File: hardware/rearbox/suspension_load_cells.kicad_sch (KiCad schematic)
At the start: 16 parts, among them U31 NAU7802SGI

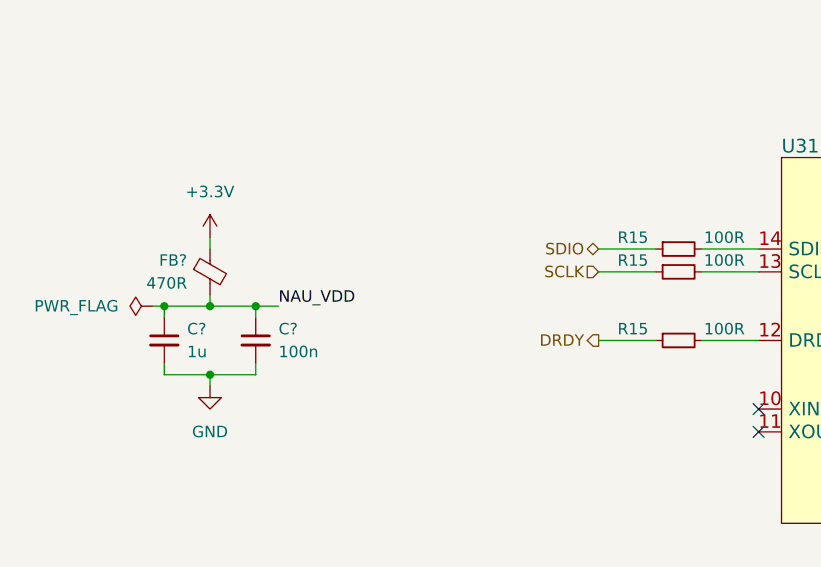
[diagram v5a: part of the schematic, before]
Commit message: Route the tracks on the connector PCB
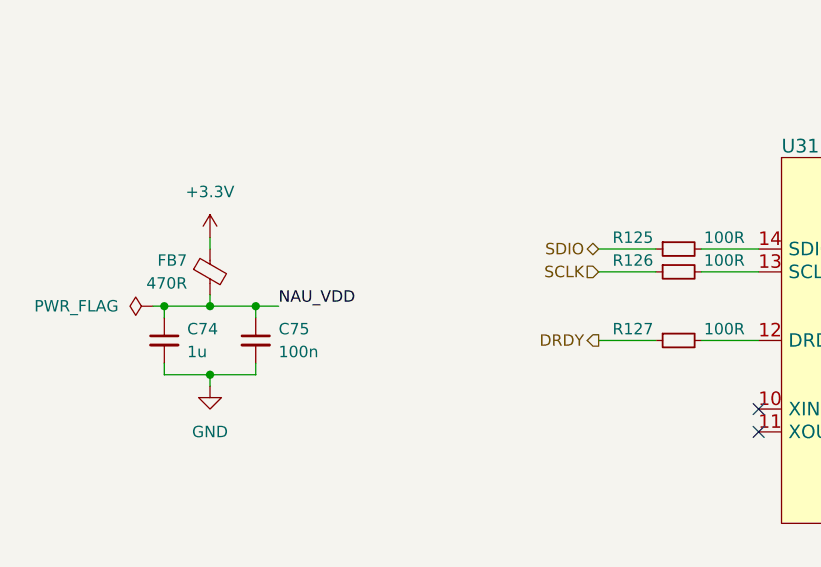
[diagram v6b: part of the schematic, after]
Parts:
- gave numbers to parts that had none: 3
- renumbered R15 to R125, R15 to R126, R15 to R127
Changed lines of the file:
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@@
   (symbol (lib_id "Device:C_Small") (at 74.93 102.87 0) (unit 1)
     (in_bom yes) (on_board yes) (dnp no)
-    (property "Reference" "C?" (at 77.47 101.6 0)
+    (property "Reference" "C75" (at 77.47 101.6 0)
       (effects (font (size 1.27 1.27)) (justify left))
     )
@@
     (instances
       (project "rearbox"
-        (path "/b652b05a-4e3d-4ad1-b032-18886abe7d45/38408e41-dfb1-4c27-acb0-3f1224cc8789"
-          (reference "C?") (unit 1)
-        )
-        (path "/b652b05a-4e3d-4ad1-b032-18886abe7d45/38408e41-dfb1-4c27-acb0-3f1224cc8789/eec2c93a-0fce-4d3a-ab43-9e1e0481c06c"
-          (reference "C28") (unit 1)
-        )
-        (path "/b652b05a-4e3d-4ad1-b032-18886abe7d45/38408e41-dfb1-4c27-acb0-3f1224cc8789/f1ed15a3-9302-436f-b25a-713477aeadf3"
-          (reference "C30") (unit 1)
-        )
         (path "/b652b05a-4e3d-4ad1-b032-18886abe7d45/ae02a5e7-3434-4bcc-98d7-f72e76418900"
           (reference "C75") (unit 1)
@@
   (symbol (lib_id "power:+3.3V") (at 69.85 91.44 0) (unit 1)
     (in_bom yes) (on_board yes) (dnp no)
-    (property "Reference" "#PWR012" (at 69.85 95.25 0)
+    (property "Reference" "#PWR0243" (at 69.85 95.25 0)
       (effects (font (size 1.27 1.27)) hide)
     )
@@
     (instances
       (project "rearbox"
-        (path "/b652b05a-4e3d-4ad1-b032-18886abe7d45"
-          (reference "#PWR012") (unit 1)
-        )
         (path "/b652b05a-4e3d-4ad1-b032-18886abe7d45/ae02a5e7-3434-4bcc-98d7-f72e76418900"
           (reference "#PWR0243") (unit 1)
@@
   (symbol (lib_id "Device:R_Small") (at 121.92 102.87 90) (mirror x) (unit 1)
     (in_bom yes) (on_board yes) (dnp no)
-    (property "Reference" "R15" (at 116.84 101.6 90)
+    (property "Reference" "R127" (at 116.84 101.6 90)
       (effects (font (size 1.27 1.27)))
     )
@@
     (instances
       (project "rearbox"
-        (path "/b652b05a-4e3d-4ad1-b032-18886abe7d45/12f12a63-cabc-40cf-a64b-d1bd8b3dd459"
-          (reference "R15") (unit 1)
-        )
-        (path "/b652b05a-4e3d-4ad1-b032-18886abe7d45/5d9671f9-6e77-4376-b4d6-afe9f66a07c2"
-          (reference "R151") (unit 1)
-        )
         (path "/b652b05a-4e3d-4ad1-b032-18886abe7d45/ae02a5e7-3434-4bcc-98d7-f72e76418900"
           (reference "R127") (unit 1)
@@
   (symbol (lib_id "Device:R_Small") (at 121.92 92.71 90) (mirror x) (unit 1)
     (in_bom yes) (on_board yes) (dnp no)
-    (property "Reference" "R15" (at 116.84 91.44 90)
+    (property "Reference" "R125" (at 116.84 91.44 90)
       (effects (font (size 1.27 1.27)))
     )
@@
     (instances
       (project "rearbox"
-        (path "/b652b05a-4e3d-4ad1-b032-18886abe7d45/12f12a63-cabc-40cf-a64b-d1bd8b3dd459"
-          (reference "R15") (unit 1)
-        )
-        (path "/b652b05a-4e3d-4ad1-b032-18886abe7d45/5d9671f9-6e77-4376-b4d6-afe9f66a07c2"
-          (reference "R151") (unit 1)
-        )
         (path "/b652b05a-4e3d-4ad1-b032-18886abe7d45/ae02a5e7-3434-4bcc-98d7-f72e76418900"
           (reference "R125") (unit 1)
@@
   (symbol (lib_id "power:GND") (at 69.85 107.95 0) (unit 1)
     (in_bom yes) (on_board yes) (dnp no)
-    (property "Reference" "#PWR?" (at 69.85 114.3 0)
+    (property "Reference" "#PWR0244" (at 69.85 114.3 0)
       (effects (font (size 1.27 1.27)) hide)
     )
@@
     (instances
       (project "rearbox"
-        (path "/b652b05a-4e3d-4ad1-b032-18886abe7d45/38408e41-dfb1-4c27-acb0-3f1224cc8789"
-          (reference "#PWR?") (unit 1)
-        )
-        (path "/b652b05a-4e3d-4ad1-b032-18886abe7d45/38408e41-dfb1-4c27-acb0-3f1224cc8789/eec2c93a-0fce-4d3a-ab43-9e1e0481c06c"
-          (reference "#PWR059") (unit 1)
-        )
-        (path "/b652b05a-4e3d-4ad1-b032-18886abe7d45/38408e41-dfb1-4c27-acb0-3f1224cc8789/f1ed15a3-9302-436f-b25a-713477aeadf3"
-          (reference "#PWR065") (unit 1)
-        )
         (path "/b652b05a-4e3d-4ad1-b032-18886abe7d45/ae02a5e7-3434-4bcc-98d7-f72e76418900"
           (reference "#PWR0244") (unit 1)
@@
   (symbol (lib_id "Device:C_Small") (at 64.77 102.87 0) (unit 1)
     (in_bom yes) (on_board yes) (dnp no)
-    (property "Reference" "C?" (at 67.31 101.6 0)
+    (property "Reference" "C74" (at 67.31 101.6 0)
       (effects (font (size 1.27 1.27)) (justify left))
     )
@@
     (instances
       (project "rearbox"
-        (path "/b652b05a-4e3d-4ad1-b032-18886abe7d45/38408e41-dfb1-4c27-acb0-3f1224cc8789"
-          (reference "C?") (unit 1)
-        )
-        (path "/b652b05a-4e3d-4ad1-b032-18886abe7d45/38408e41-dfb1-4c27-acb0-3f1224cc8789/eec2c93a-0fce-4d3a-ab43-9e1e0481c06c"
-          (reference "C28") (unit 1)
-        )
-        (path "/b652b05a-4e3d-4ad1-b032-18886abe7d45/38408e41-dfb1-4c27-acb0-3f1224cc8789/f1ed15a3-9302-436f-b25a-713477aeadf3"
-          (reference "C30") (unit 1)
-        )
         (path "/b652b05a-4e3d-4ad1-b032-18886abe7d45/ae02a5e7-3434-4bcc-98d7-f72e76418900"
           (reference "C74") (unit 1)
@@
   (symbol (lib_id "power:PWR_FLAG") (at 63.5 99.06 90) (unit 1)
     (in_bom yes) (on_board yes) (dnp no)
-    (property "Reference" "#FLG012" (at 61.595 99.06 0)
+    (property "Reference" "#FLG016" (at 61.595 99.06 0)
       (effects (font (size 1.27 1.27)) hide)
     )
@@
     (instances
       (project "rearbox"
-        (path "/b652b05a-4e3d-4ad1-b032-18886abe7d45/38408e41-dfb1-4c27-acb0-3f1224cc8789/f1ed15a3-9302-436f-b25a-713477aeadf3"
-          (reference "#FLG012") (unit 1)
-        )
-        (path "/b652b05a-4e3d-4ad1-b032-18886abe7d45/38408e41-dfb1-4c27-acb0-3f1224cc8789/eec2c93a-0fce-4d3a-ab43-9e1e0481c06c"
-          (reference "#FLG010") (unit 1)
-        )
         (path "/b652b05a-4e3d-4ad1-b032-18886abe7d45/ae02a5e7-3434-4bcc-98d7-f72e76418900"
           (reference "#FLG016") (unit 1)
@@
   (symbol (lib_id "Device:FerriteBead_Small") (at 69.85 95.25 0) (unit 1)
     (in_bom yes) (on_board yes) (dnp no)
-    (property "Reference" "FB?" (at 67.31 93.98 0)
+    (property "Reference" "FB7" (at 67.31 93.98 0)
       (effects (font (size 1.27 1.27)) (justify right))
     )
@@
     (instances
       (project "rearbox"
-        (path "/b652b05a-4e3d-4ad1-b032-18886abe7d45/38408e41-dfb1-4c27-acb0-3f1224cc8789"
-          (reference "FB?") (unit 1)
-        )
-        (path "/b652b05a-4e3d-4ad1-b032-18886abe7d45/38408e41-dfb1-4c27-acb0-3f1224cc8789/eec2c93a-0fce-4d3a-ab43-9e1e0481c06c"
-          (reference "FB3") (unit 1)
-        )
-        (path "/b652b05a-4e3d-4ad1-b032-18886abe7d45/38408e41-dfb1-4c27-acb0-3f1224cc8789/f1ed15a3-9302-436f-b25a-713477aeadf3"
-          (reference "FB5") (unit 1)
-        )
         (path "/b652b05a-4e3d-4ad1-b032-18886abe7d45/ae02a5e7-3434-4bcc-98d7-f72e76418900"
           (reference "FB7") (unit 1)
@@
   (symbol (lib_id "power:GND") (at 146.05 128.27 0) (unit 1)
     (in_bom yes) (on_board yes) (dnp no)
-    (property "Reference" "#PWR?" (at 146.05 134.62 0)
+    (property "Reference" "#PWR0245" (at 146.05 134.62 0)
       (effects (font (size 1.27 1.27)) hide)
     )
@@
     (instances
       (project "rearbox"
-        (path "/b652b05a-4e3d-4ad1-b032-18886abe7d45"
-          (reference "#PWR?") (unit 1)
-        )
-        (path "/b652b05a-4e3d-4ad1-b032-18886abe7d45/5d9671f9-6e77-4376-b4d6-afe9f66a07c2"
-          (reference "#PWR0107") (unit 1)
-        )
         (path "/b652b05a-4e3d-4ad1-b032-18886abe7d45/ae02a5e7-3434-4bcc-98d7-f72e76418900"
           (reference "#PWR0245") (unit 1)
@@
   (symbol (lib_id "Device:R_Small") (at 121.92 95.25 90) (mirror x) (unit 1)
     (in_bom yes) (on_board yes) (dnp no)
-    (property "Reference" "R15" (at 116.84 93.98 90)
+    (property "Reference" "R126" (at 116.84 93.98 90)
       (effects (font (size 1.27 1.27)))
     )
@@
     (instances
       (project "rearbox"
-        (path "/b652b05a-4e3d-4ad1-b032-18886abe7d45/12f12a63-cabc-40cf-a64b-d1bd8b3dd459"
-          (reference "R15") (unit 1)
-        )
-        (path "/b652b05a-4e3d-4ad1-b032-18886abe7d45/5d9671f9-6e77-4376-b4d6-afe9f66a07c2"
-          (reference "R151") (unit 1)
-        )
         (path "/b652b05a-4e3d-4ad1-b032-18886abe7d45/ae02a5e7-3434-4bcc-98d7-f72e76418900"
           (reference "R126") (unit 1)
@@
   (symbol (lib_id "Power_Ports:+3V_EXT") (at 179.07 114.3 0) (unit 1)
     (in_bom yes) (on_board yes) (dnp no)
-    (property "Reference" "PWR01" (at 179.07 109.22 0)
+    (property "Reference" "#PWR0248" (at 179.07 109.22 0)
       (effects (font (size 1.27 1.27)) hide)
     )
@@
     (instances
       (project "rearbox"
-        (path "/b652b05a-4e3d-4ad1-b032-18886abe7d45/7045152e-d7a2-42d7-9b15-138e7f2928ca"
-          (reference "PWR01") (unit 1)
-        )
         (path "/b652b05a-4e3d-4ad1-b032-18886abe7d45/ae02a5e7-3434-4bcc-98d7-f72e76418900"
           (reference "#PWR0248") (unit 1)

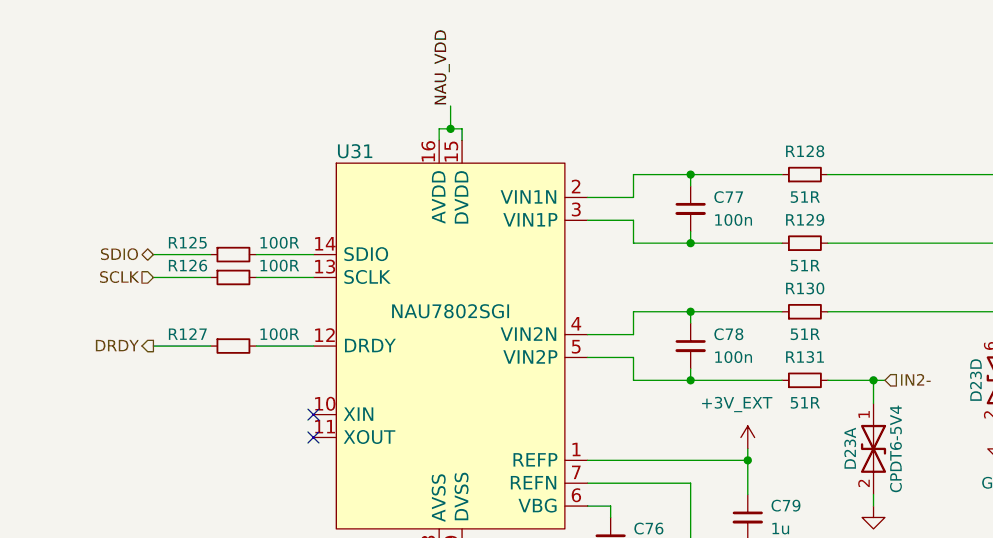
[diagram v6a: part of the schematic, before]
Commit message: Fix measurement bridges polarity
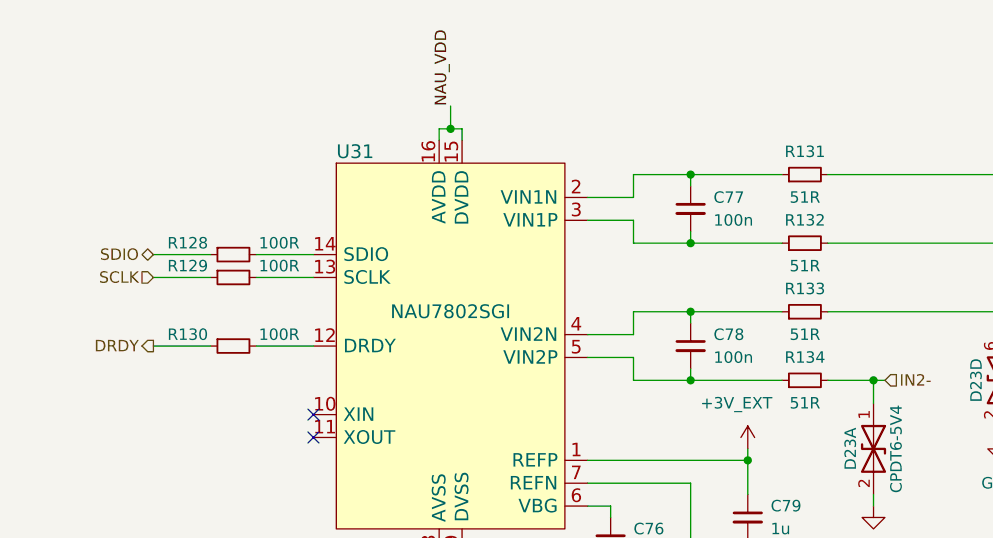
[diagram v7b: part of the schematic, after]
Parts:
- renumbered R125 to R128, R126 to R129, R127 to R130, R128 to R131, R129 to R132, R130 to R133, R131 to R134
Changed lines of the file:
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@@
   (title_block
     (title "Suspension Load Cells")
-    (date "2023-11-17")
+    (date "2024-04-28")
     (rev "${REVISION}")
     (company "Author: I. Kajdan")
@@
   (symbol (lib_id "Device:R_Small") (at 185.42 83.82 90) (unit 1)
     (in_bom yes) (on_board yes) (dnp no)
-    (property "Reference" "R128" (at 185.42 81.28 90)
+    (property "Reference" "R131" (at 185.42 81.28 90)
       (effects (font (size 1.27 1.27)))
     )
@@
       (project "rearbox"
         (path "/b652b05a-4e3d-4ad1-b032-18886abe7d45/ae02a5e7-3434-4bcc-98d7-f72e76418900"
-          (reference "R128") (unit 1)
+          (reference "R131") (unit 1)
         )
       )
@@
   (symbol (lib_id "Device:R_Small") (at 185.42 99.06 90) (unit 1)
     (in_bom yes) (on_board yes) (dnp no)
-    (property "Reference" "R130" (at 185.42 96.52 90)
+    (property "Reference" "R133" (at 185.42 96.52 90)
       (effects (font (size 1.27 1.27)))
     )
@@
       (project "rearbox"
         (path "/b652b05a-4e3d-4ad1-b032-18886abe7d45/ae02a5e7-3434-4bcc-98d7-f72e76418900"
-          (reference "R130") (unit 1)
+          (reference "R133") (unit 1)
         )
       )
@@
   (symbol (lib_id "Device:R_Small") (at 185.42 106.68 90) (unit 1)
     (in_bom yes) (on_board yes) (dnp no)
-    (property "Reference" "R131" (at 185.42 104.14 90)
+    (property "Reference" "R134" (at 185.42 104.14 90)
       (effects (font (size 1.27 1.27)))
     )
@@
       (project "rearbox"
         (path "/b652b05a-4e3d-4ad1-b032-18886abe7d45/ae02a5e7-3434-4bcc-98d7-f72e76418900"
-          (reference "R131") (unit 1)
+          (reference "R134") (unit 1)
         )
       )
@@
   (symbol (lib_id "power:+3.3V") (at 69.85 91.44 0) (unit 1)
     (in_bom yes) (on_board yes) (dnp no)
-    (property "Reference" "#PWR0243" (at 69.85 95.25 0)
+    (property "Reference" "#PWR0246" (at 69.85 95.25 0)
       (effects (font (size 1.27 1.27)) hide)
     )
@@
       (project "rearbox"
         (path "/b652b05a-4e3d-4ad1-b032-18886abe7d45/ae02a5e7-3434-4bcc-98d7-f72e76418900"
-          (reference "#PWR0243") (unit 1)
+          (reference "#PWR0246") (unit 1)
         )
       )
@@
   (symbol (lib_id "Device:R_Small") (at 121.92 102.87 90) (mirror x) (unit 1)
     (in_bom yes) (on_board yes) (dnp no)
-    (property "Reference" "R127" (at 116.84 101.6 90)
+    (property "Reference" "R130" (at 116.84 101.6 90)
       (effects (font (size 1.27 1.27)))
     )
@@
       (project "rearbox"
         (path "/b652b05a-4e3d-4ad1-b032-18886abe7d45/ae02a5e7-3434-4bcc-98d7-f72e76418900"
-          (reference "R127") (unit 1)
+          (reference "R130") (unit 1)
         )
       )
@@
   (symbol (lib_id "power:GND") (at 172.72 128.27 0) (unit 1)
     (in_bom yes) (on_board yes) (dnp no) (fields_autoplaced)
-    (property "Reference" "#PWR0247" (at 172.72 134.62 0)
+    (property "Reference" "#PWR0250" (at 172.72 134.62 0)
       (effects (font (size 1.27 1.27)) hide)
     )
@@
       (project "rearbox"
         (path "/b652b05a-4e3d-4ad1-b032-18886abe7d45/ae02a5e7-3434-4bcc-98d7-f72e76418900"
-          (reference "#PWR0247") (unit 1)
+          (reference "#PWR0250") (unit 1)
         )
       )
@@
   (symbol (lib_id "power:GND") (at 207.01 113.03 0) (unit 1)
     (in_bom yes) (on_board yes) (dnp no) (fields_autoplaced)
-    (property "Reference" "#PWR0251" (at 207.01 119.38 0)
+    (property "Reference" "#PWR0254" (at 207.01 119.38 0)
       (effects (font (size 1.27 1.27)) hide)
     )
@@
       (project "rearbox"
         (path "/b652b05a-4e3d-4ad1-b032-18886abe7d45/ae02a5e7-3434-4bcc-98d7-f72e76418900"
-          (reference "#PWR0251") (unit 1)
+          (reference "#PWR0254") (unit 1)
         )
       )
@@
   (symbol (lib_id "Device:R_Small") (at 121.92 92.71 90) (mirror x) (unit 1)
     (in_bom yes) (on_board yes) (dnp no)
-    (property "Reference" "R125" (at 116.84 91.44 90)
+    (property "Reference" "R128" (at 116.84 91.44 90)
       (effects (font (size 1.27 1.27)))
     )
@@
       (project "rearbox"
         (path "/b652b05a-4e3d-4ad1-b032-18886abe7d45/ae02a5e7-3434-4bcc-98d7-f72e76418900"
-          (reference "R125") (unit 1)
+          (reference "R128") (unit 1)
         )
       )
@@
   (symbol (lib_id "power:GND") (at 179.07 128.27 0) (unit 1)
     (in_bom yes) (on_board yes) (dnp no) (fields_autoplaced)
-    (property "Reference" "#PWR0249" (at 179.07 134.62 0)
+    (property "Reference" "#PWR0252" (at 179.07 134.62 0)
       (effects (font (size 1.27 1.27)) hide)
     )
@@
       (project "rearbox"
         (path "/b652b05a-4e3d-4ad1-b032-18886abe7d45/ae02a5e7-3434-4bcc-98d7-f72e76418900"
-          (reference "#PWR0249") (unit 1)
+          (reference "#PWR0252") (unit 1)
         )
       )
@@
   (symbol (lib_id "power:GND") (at 69.85 107.95 0) (unit 1)
     (in_bom yes) (on_board yes) (dnp no)
-    (property "Reference" "#PWR0244" (at 69.85 114.3 0)
+    (property "Reference" "#PWR0247" (at 69.85 114.3 0)
       (effects (font (size 1.27 1.27)) hide)
     )
@@
       (project "rearbox"
         (path "/b652b05a-4e3d-4ad1-b032-18886abe7d45/ae02a5e7-3434-4bcc-98d7-f72e76418900"
-          (reference "#PWR0244") (unit 1)
+          (reference "#PWR0247") (unit 1)
         )
       )
@@
   (symbol (lib_id "power:GND") (at 220.98 105.41 0) (unit 1)
     (in_bom yes) (on_board yes) (dnp no) (fields_autoplaced)
-    (property "Reference" "#PWR0252" (at 220.98 111.76 0)
+    (property "Reference" "#PWR0255" (at 220.98 111.76 0)
       (effects (font (size 1.27 1.27)) hide)
     )
@@
       (project "rearbox"
         (path "/b652b05a-4e3d-4ad1-b032-18886abe7d45/ae02a5e7-3434-4bcc-98d7-f72e76418900"
-          (reference "#PWR0252") (unit 1)
+          (reference "#PWR0255") (unit 1)
         )
       )
@@
   (symbol (lib_id "power:GND") (at 193.04 120.65 0) (unit 1)
     (in_bom yes) (on_board yes) (dnp no) (fields_autoplaced)
-    (property "Reference" "#PWR0250" (at 193.04 127 0)
+    (property "Reference" "#PWR0253" (at 193.04 127 0)
       (effects (font (size 1.27 1.27)) hide)
     )
@@
       (project "rearbox"
         (path "/b652b05a-4e3d-4ad1-b032-18886abe7d45/ae02a5e7-3434-4bcc-98d7-f72e76418900"
-          (reference "#PWR0250") (unit 1)
+          (reference "#PWR0253") (unit 1)
         )
       )
@@
   (symbol (lib_id "Device:R_Small") (at 185.42 91.44 90) (unit 1)
     (in_bom yes) (on_board yes) (dnp no)
-    (property "Reference" "R129" (at 185.42 88.9 90)
+    (property "Reference" "R132" (at 185.42 88.9 90)
       (effects (font (size 1.27 1.27)))
     )
@@
       (project "rearbox"
         (path "/b652b05a-4e3d-4ad1-b032-18886abe7d45/ae02a5e7-3434-4bcc-98d7-f72e76418900"
-          (reference "R129") (unit 1)
+          (reference "R132") (unit 1)
         )
       )
@@
   (symbol (lib_id "power:GND") (at 163.83 128.27 0) (unit 1)
     (in_bom yes) (on_board yes) (dnp no) (fields_autoplaced)
-    (property "Reference" "#PWR0246" (at 163.83 134.62 0)
+    (property "Reference" "#PWR0249" (at 163.83 134.62 0)
       (effects (font (size 1.27 1.27)) hide)
     )
@@
       (project "rearbox"
         (path "/b652b05a-4e3d-4ad1-b032-18886abe7d45/ae02a5e7-3434-4bcc-98d7-f72e76418900"
-          (reference "#PWR0246") (unit 1)
+          (reference "#PWR0249") (unit 1)
         )
       )
@@
   (symbol (lib_id "power:GND") (at 146.05 128.27 0) (unit 1)
     (in_bom yes) (on_board yes) (dnp no)
-    (property "Reference" "#PWR0245" (at 146.05 134.62 0)
+    (property "Reference" "#PWR0248" (at 146.05 134.62 0)
       (effects (font (size 1.27 1.27)) hide)
     )
@@
       (project "rearbox"
         (path "/b652b05a-4e3d-4ad1-b032-18886abe7d45/ae02a5e7-3434-4bcc-98d7-f72e76418900"
-          (reference "#PWR0245") (unit 1)
+          (reference "#PWR0248") (unit 1)
         )
       )
@@
   (symbol (lib_id "Device:R_Small") (at 121.92 95.25 90) (mirror x) (unit 1)
     (in_bom yes) (on_board yes) (dnp no)
-    (property "Reference" "R126" (at 116.84 93.98 90)
+    (property "Reference" "R129" (at 116.84 93.98 90)
       (effects (font (size 1.27 1.27)))
     )
@@
       (project "rearbox"
         (path "/b652b05a-4e3d-4ad1-b032-18886abe7d45/ae02a5e7-3434-4bcc-98d7-f72e76418900"
-          (reference "R126") (unit 1)
+          (reference "R129") (unit 1)
         )
       )
@@
   (symbol (lib_id "Power_Ports:+3V_EXT") (at 179.07 114.3 0) (unit 1)
     (in_bom yes) (on_board yes) (dnp no)
-    (property "Reference" "#PWR0248" (at 179.07 109.22 0)
+    (property "Reference" "#PWR0251" (at 179.07 109.22 0)
       (effects (font (size 1.27 1.27)) hide)
     )
@@
       (project "rearbox"
         (path "/b652b05a-4e3d-4ad1-b032-18886abe7d45/ae02a5e7-3434-4bcc-98d7-f72e76418900"
-          (reference "#PWR0248") (unit 1)
+          (reference "#PWR0251") (unit 1)
         )
       )
@@
   (symbol (lib_id "power:GND") (at 234.95 97.79 0) (unit 1)
     (in_bom yes) (on_board yes) (dnp no) (fields_autoplaced)
-    (property "Reference" "#PWR0253" (at 234.95 104.14 0)
+    (property "Reference" "#PWR0256" (at 234.95 104.14 0)
       (effects (font (size 1.27 1.27)) hide)
     )
@@
       (project "rearbox"
         (path "/b652b05a-4e3d-4ad1-b032-18886abe7d45/ae02a5e7-3434-4bcc-98d7-f72e76418900"
-          (reference "#PWR0253") (unit 1)
-        )
-      )
+          (reference "#PWR0256") (unit 1)
+        )
+      )
